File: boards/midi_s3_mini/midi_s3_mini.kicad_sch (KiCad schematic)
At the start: 35 parts, among them J1 Power2, J10 PLAY_CUE, J11 JOG, J12 TEMPO, J2 Power1, J3 UART_PI, J4 OneButtonA_TX, J5 OneButtonA_RX, J6 OneButtonB_RX, J7 OneButtonB_TX, J8 LOOP, J9 TRACK_ENC, U1 LOLIN_S3_Mini

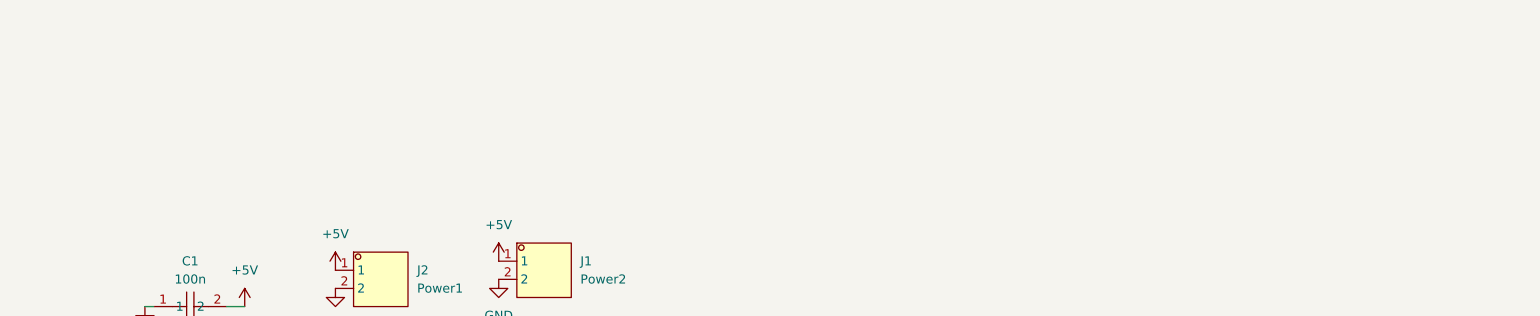
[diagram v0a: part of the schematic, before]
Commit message: Add notes and update schematic for main board ESD Schotky fix jog tch
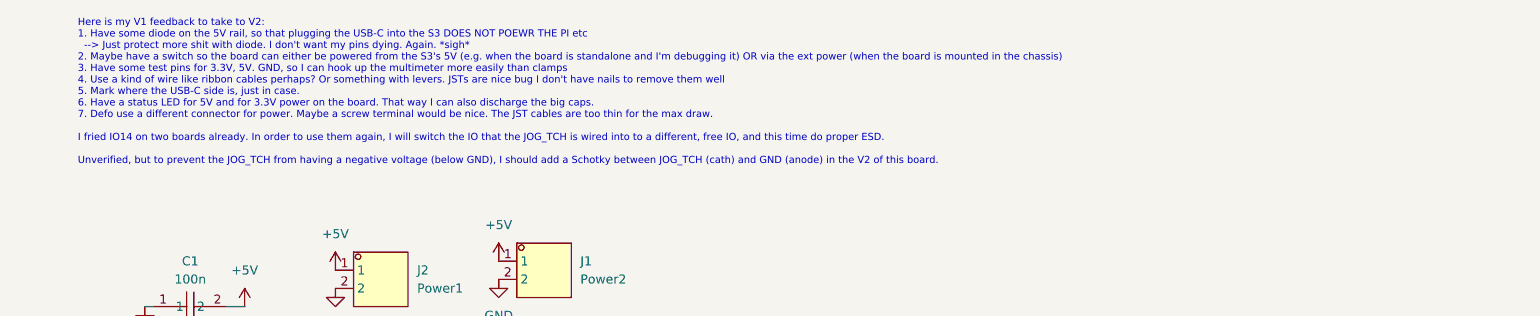
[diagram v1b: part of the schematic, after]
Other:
- note added: "Here is my V1 feedback to take to V2: 1. Have some diode on the 5V rail, so that plugging the USB-C into the S3 DOES NOT POEWR THE PI etc --> Just protect more shit with diode. I don't want my pins dying. Again. *sigh* 2. Maybe have a switch so the board can either be powered from the S3's 5V (e.g. when the board is standalone and I'm debugging it) OR via the ext power (when the board is mounted 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"
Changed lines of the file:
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@@
+		)
+	)
+	(text "Here is my V1 feedback to take to V2:\n1. Have some diode on the 5V rail, so that plugging the USB-C into the S3 DOES NOT POEWR THE PI etc\n  --> Just protect more shit with diode. I don't want my pins dying. Again. *sigh*\n2. Maybe have a switch so the board can either be powered from the S3's 5V (e.g. when the board is standalone and I'm debugging it) OR via the ext power (when the board is mounted in the chassis)\n3. Have some test pins for 3.3V, 5V. GND, so I can hook up the multimeter more easily than clamps\n4. Use a kind of wire like ribbon cables perhaps? Or something with levers. JSTs are nice bug I don't have nails to remove them well\n5. Mark where the USB-C side is, just in case.\n6. Have a status LED for 5V and for 3.3V power on the board. That way I can also discharge the big caps.\n7. Defo use a different connector for power. Maybe a screw terminal would be nice. The JST cables are too thin for the max draw.\n\nI fried IO14 on two boards already. In order to use them again, I will switch the IO that the JOG_TCH is wired into to a different, free IO, and this time do proper ESD.\n\nUnverified, but to prevent the JOG_TCH from having a negative voltage (below GND), I should add a Schotky between JOG_TCH (cath) and GND (anode) in the V2 of this board."
+		(exclude_from_sim no)
+		(at 24.892 -5.842 0)
+		(effects
+			(font
+				(size 1 1)
+			)
+			(justify left)
 		)
 	)

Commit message: Design the new power supply system
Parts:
- removed C1, C3: 100n, easyeda2kicad:CAP-TH_L4.2-W3.5-P2.54-D0.5, symbol easyeda2kicad:178MU0006
- removed C2: 1000uF / 35 V, easyeda2kicad:CAP-TH_BD10.0-P5.00-D1.0-FD, symbol easyeda2kicad:ERR1VM102G20OT
- removed C5: 10u / 50 V, easyeda2kicad:CAP-TH_BD5.0-P2.00-D0.8-FD, symbol easyeda2kicad:01EC1809SHC10UF50V
- removed C6: 22u 50V, easyeda2kicad:CAP-TH_BD5.0-P2.00-D0.5-FD, symbol easyeda2kicad:ERG50V22M5X11
- removed J1: Power2, easyeda2kicad:CONN-TH_S2B-PH-K-S-LF-SN, symbol easyeda2kicad:S2B-PH-K-S
- removed J2: Power1, easyeda2kicad:CONN-TH_S2B-PH-K-S-LF-SN, symbol easyeda2kicad:S2B-PH-K-S
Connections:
- net +3.3V: no longer U1.8 (3V3)
- net +5V: no longer U1.32 (VBUS)
- net JOG_TCH: no longer U1.16 (IO14)
- new net S3_3.3V: U1.8 (3V3)
- new net S3_VBUS_5V: U1.32 (VBUS)
- no-connect marks 5 -> 6
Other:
- added sheet Power (power.kicad_sch)
- note added: "I burnt IO14 on some boards, so for flexibility I will not use it"
- moved on the sheet: C4

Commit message: Add test points and leds
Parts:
- added TP3: VBUS_S3, symbol Connector:TestPoint
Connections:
- net S3_VBUS_5V: now also TP3.1
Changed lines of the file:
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@@
 		(color 0 0 0 0)
 	)
+	(junction
+		(at 134.62 78.74)
+		(diameter 0)
+		(color 0 0 0 0)
+	)
 	(no_connect
 		(at 100.33 78.74)
@@
 	(wire
 		(pts
+			(xy 134.62 78.74) (xy 133.35 78.74)
+		)
+		(stroke
+			(width 0)
+			(type default)
+		)
+	)
+	(wire
+		(pts
 			(xy 179.07 114.3) (xy 179.07 116.84)
 		)
@@
 	(wire
 		(pts
+			(xy 134.62 80.01) (xy 134.62 78.74)
+		)
+		(stroke
+			(width 0)
+			(type default)
+		)
+	)
+	(wire
+		(pts
 			(xy 69.85 129.54) (xy 72.39 129.54)
 		)
@@
 	(wire
 		(pts
+			(xy 135.89 78.74) (xy 134.62 78.74)
+		)
+		(stroke
+			(width 0)
+			(type default)
+		)
+	)
+	(wire
+		(pts
 			(xy 214.63 86.36) (xy 220.98 86.36)
 		)
@@
 	(global_label "S3_VBUS_5V"
 		(shape input)
-		(at 133.35 78.74 0)
+		(at 135.89 78.74 0)
 		(fields_autoplaced yes)
 		(effects
@@
 		)
 		(property "Intersheetrefs" "${INTERSHEET_REFS}"
-			(at 147.8861 78.74 0)
+			(at 150.4261 78.74 0)
 			(hide yes)
 			(show_name no)
@@
 					(unit 1)
 				)
+			)
+		)
+	)
+	(symbol
+		(lib_id "Connector:TestPoint")
+		(at 134.62 80.01 180)
+		(unit 1)
+		(body_style 1)
+		(exclude_from_sim no)
+		(in_bom yes)
+		(on_board yes)
+		(in_pos_files yes)
+		(dnp no)
+		(fields_autoplaced yes)
+		(property "Reference" "TP3"
+			(at 137.16 82.0419 0)
+			(show_name no)
+			(do_not_autoplace no)
+			(effects
+				(font
+					(size 1.27 1.27)
+				)
+				(justify right)
+			)
+		)
+		(property "Value" "VBUS_S3"
+			(at 137.16 84.5819 0)
+			(show_name no)
+			(do_not_autoplace no)
+			(effects
+				(font
+					(size 1.27 1.27)
+				)
+				(justify right)
+			)
+		)
+		(property "Footprint" ""
+			(at 129.54 80.01 0)
+			(hide yes)
+			(show_name no)
+			(do_not_autoplace no)
+			(effects
+				(font
+					(size 1.27 1.27)
+				)
+			)
+		)
+		(property "Datasheet" ""
+			(at 129.54 80.01 0)
+			(hide yes)
+			(show_name no)
+			(do_not_autoplace no)
+			(effects
+				(font
+					(size 1.27 1.27)
+				)
+			)
+		)
+		(property "Description" "test point"
+			(at 134.62 80.01 0)
+			(hide yes)
+			(show_name no)
+			(do_not_autoplace no)
+			(effects
+				(font
+					(size 1.27 1.27)
+				)
+			)
+		)
+		(pin "1"
+		)
+		(instances
+			(project "midi_s3_mini"
+				(path "/4a4c0c1b-df1c-48df-9685-1cfae0dce3a5"
+					(reference "TP3")
+					(unit 1)
+				)

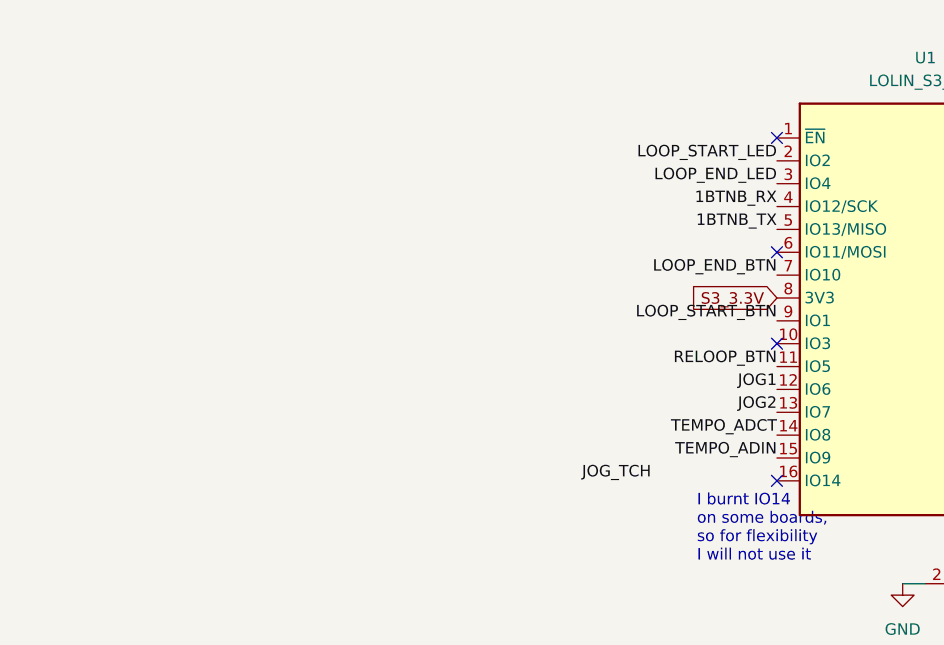
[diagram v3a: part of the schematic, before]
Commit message: Reassign JOG_TCH from IO14 --> IO11 on V2 boards
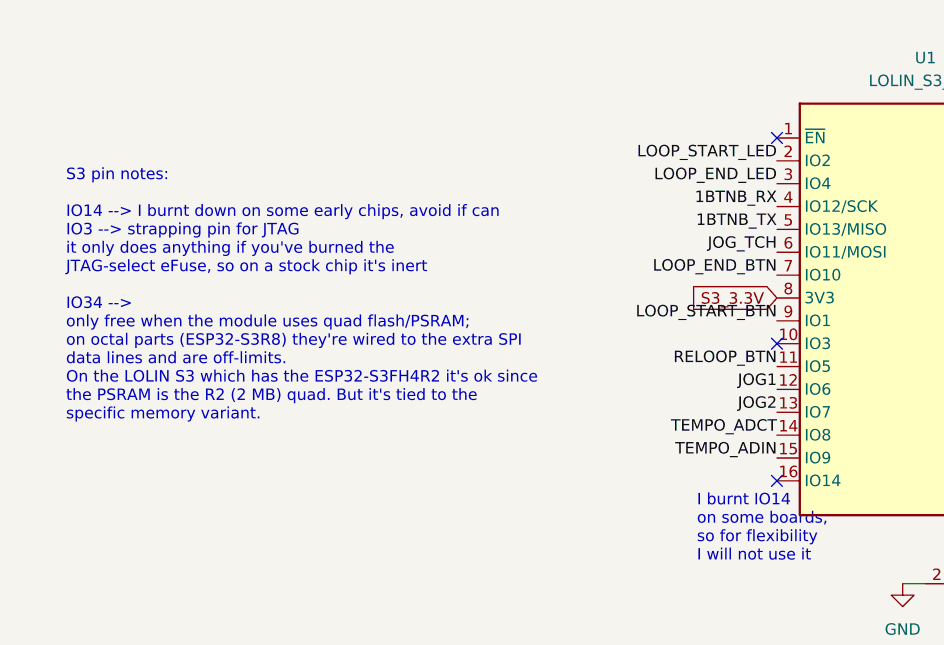
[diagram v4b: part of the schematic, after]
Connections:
- net JOG_TCH: now also U1.6 (IO11/MOSI)
- no-connect marks 6 -> 5
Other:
- note added: "S3 pin notes: IO14 --> I burnt down on some early chips, avoid if can IO3 --> strapping pin for JTAG it only does anything if you've burned the JTAG-select eFuse, so on a stock chip it's inert IO34 --> only free when the module uses quad flash/PSRAM; on octal parts (ESP32-S3R8) they're wired to the extra SPI data lines and are off-limits. On the LOLIN S3 which has the ESP32-S3FH4R2 it's ok since 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"
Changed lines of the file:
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@@
+		)
+	)
+	(text "S3 pin notes:\n\nIO14 --> I burnt down on some early chips, avoid if can\nIO3 --> strapping pin for JTAG\nit only does anything if you've burned the \nJTAG-select eFuse, so on a stock chip it's inert\n\nIO34 --> \nonly free when the module uses quad flash/PSRAM; \non octal parts (ESP32-S3R8) they're wired to the extra SPI \ndata lines and are off-limits.\nOn the LOLIN S3 which has the ESP32-S3FH4R2 it's ok since \nthe PSRAM is the R2 (2 MB) quad. But it's tied to the \nspecific memory variant. "
+		(exclude_from_sim no)
+		(at 21.336 58.166 0)
+		(effects
+			(font
+				(size 1.27 1.27)
+			)
+			(justify left)
 		)
 	)
@@
 	)
 	(no_connect
-		(at 100.33 53.34)
-	)
-	(no_connect
 		(at 133.35 73.66)
 	)
@@
 		)
 	)
+	(label "JOG_TCH"
+		(at 100.33 53.34 180)
+		(effects
+			(font
+				(size 1.27 1.27)
+			)
+			(justify right bottom)
+		)
+	)
 	(label "LED_CUE"
 		(at 133.35 133.35 180)
@@
 		(effects
 			(font
-				(size 1.27 1.27)
-			)
-			(justify right bottom)
-		)
-	)
-	(label "JOG_TCH"
-		(at 86.36 78.74 180)
-		(effects
-			(font

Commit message: Finish the ESD and power system for the V2 midi S3
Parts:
- removed C10, C11, C12, C13, C4, C7, C9: 100n, easyeda2kicad:CAP-TH_L4.2-W3.5-P2.54-D0.5, symbol easyeda2kicad:178MU0006
- removed J11: JOG, easyeda2kicad:CONN-TH_S5B-PH-K-S-LF-SN, symbol easyeda2kicad:S5B-PH-K-S-
- removed J3: UART_PI, easyeda2kicad:CONN-TH_3P-P2.00_S3B-PH-K-S-LF-SN, symbol easyeda2kicad:S3B-PH-K-S-
- added C10, C11, C2, C3, C5, C6, C8, C9: 100n s, easyeda2kicad:C0402, symbol easyeda2kicad:CL05B104KB54PNC
- added C4: 10nF ±10% 50V, easyeda2kicad:C0402, symbol easyeda2kicad:CL05B103KB5NNNC
- added J10: JOG, easyeda2kicad:CONN-TH_S5B-PH-K-S-LF-SN, symbol easyeda2kicad:S5B-PH-K-S-
- added J5: UART_PI, easyeda2kicad:CONN-TH_4P-P2.00_S4B-PH-K-S-LF-SN, symbol easyeda2kicad:S4B-PH-K-S-
- added R1, R10, R11, R12, R13, R14, R15, R16, R18, R19, R2, R20, R21, R22, R23, R24, R25, R26, R7, R8, R9: 1KΩ ±1%, easyeda2kicad:R0402, symbol easyeda2kicad:0402WGF1001TCE
- added TVS1, TVS2, TVS3, TVS4, TVS5, TVS6, TVS7, TVS8: SRV05-4, easyeda2kicad:SOT-23-6_L2.9-W1.6-P0.95-LS2.8-BL, symbol easyeda2kicad:SRV05-4_C558418
- renumbered C8 to C7, J4 to J1, J5 to J2, J6 to J3, J7 to J4, J9 to J6, J8 to J7, J10 to J8, J12 to J9, R5 to R17, R1 to R3, R2 to R4, R3 to R5, R4 to R6, TP3 to TP1
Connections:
- net +3.3V: now also C2.2, C6.2, C9.2, J10.3, TVS1.5, TVS2.5, TVS3.5, TVS4.5, TVS5.5, TVS6.5, TVS7.5, TVS8.5
- net +5V: now also C11.2
- net 1BTNA_RX: now also TVS1.1, TVS1.3
- net 1BTNA_TX: now also R1.1; no longer J1.2
- net 1BTNB_TX: now also R2.1; no longer J4.2
- net BTN_CUE: now also R21.1; no longer J8.4
- net BTN_PLAY: now also R18.1; no longer J8.2
- net ENC_CLK: now also C3.2, R12.1; no longer J6.5
- net ENC_DT: now also C5.2, R10.1; no longer J6.4
- net ENC_SW: now also C4.2, R9.1; no longer J6.3
- net GND: now also C10.1, C11.1, C2.1, C3.1, C4.1, C5.1, C6.1, C8.2, C9.1, J10.2, J5.1, J5.4, TVS1.2, TVS2.2, TVS3.2, TVS4.2, TVS5.2, TVS6.2, TVS7.2, TVS8.2
- net JOG1: now also R25.1
- net JOG2: now also R24.1
- net JOG_TCH: now also R20.1
- net LED_CUE: now also R22.1; no longer J8.5
- net LED_PLAY: now also R19.1; no longer J8.3
- net LOOP_END_BTN: now also R14.1; no longer J7.4
- net LOOP_END_LED: now also R15.1; no longer J7.5
- net LOOP_START_BTN: now also R11.1; no longer J7.2
- net LOOP_START_LED: now also R13.1; no longer J7.3
- net RELOOP_BTN: now also R16.1, TVS7.1; no longer J7.6
- net TEMPO_ADCT: now also C10.2, R26.1; no longer J9.2
- net TEMPO_ADIN: now also C8.1, R23.1; no longer J9.3
- net UART_RX_FROM_PI: now also R8.1
- net UART_TX_TO_PI: now also R7.1
- new net RAW_1BTNA_TX: J1.2, R1.2, TVS1.4
- new net RAW_1BTNB_TX: J4.2, R2.2, TVS1.6
- new net RAW_BTN_CUE: J8.4, R21.2, TVS8.3
- new net RAW_BTN_PLAY: J8.2, R18.2, TVS8.6
- new net RAW_ENC_CLK: J6.5, R12.2, TVS3.3
- new net RAW_ENC_DT: J6.4, R10.2, TVS3.6
- new net RAW_ENC_SW: J6.3, R9.2, TVS3.1
- new net RAW_JOG1: J10.5, R25.2, TVS6.1
- new net RAW_JOG2: J10.4, R24.2, TVS6.4
- new net RAW_JOG_TCH: J10.1, R20.2, TVS6.6
- new net RAW_LED_CUE: J8.5, R22.2, TVS8.1
- new net RAW_LED_PLAY: J8.3, R19.2, TVS8.4
- new net RAW_LOOP_END_BTN: J7.4, R14.2, TVS4.1
- new net RAW_LOOP_END_LED: J7.5, R15.2, TVS5.6
- new net RAW_LOOP_START_BTN: J7.2, R11.2, TVS4.6
- new net RAW_LOOP_START_LED: J7.3, R13.2, TVS5.4
- new net RAW_RELOOP_BTN: J7.6, R16.2, TVS4.4
- new net RAW_TEMPO_ADCT: J9.2, R26.2, TVS7.4
- new net RAW_TEMPO_ADIN: J9.3, R23.2, TVS7.6
- new net RAW_UART_RX_FROM_PI: J5.3, R8.2, TVS2.6
- new net RAW_UART_TX_TO_PI: J5.2, R7.2, TVS2.4
- no-connect marks 5 -> 13
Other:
- note added: "The LED_* here are controlling a MOSFET 2N7000's gate on the other side. They operate at 3.3V. The BTN_* on the other side are just a 100nF debounce cap and they close to GND, so we pull them up to 3.3V. The 5V is to power the LED, and the MOSFET open/closes the GND path on the power."
- note added: "This pinout matches the encoder's pinout if I mount a JST-PH angled on its bottom side. Enc is a KY-040"
- note removed: "This pinout matches the encoder's pinout if I mount a JST-PH angled on its bottom side"
- moved on the sheet: C7, J1, J2, J3, J4, J6, J7, J8, J9, R17, R3, R4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

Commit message: Footprint assignment for SMD assy
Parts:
- removed C7: 100n, easyeda2kicad:CAP-TH_L4.2-W3.5-P2.54-D0.5, symbol easyeda2kicad:178MU0006
- removed R17: 10k, easyeda2kicad:RES-TH_BD2.5-L6.5-P10.50-D0.6, symbol easyeda2kicad:MFR0W4F1002A50
- removed R3, R5: 1.8k, easyeda2kicad:RES-TH_BD2.4-L6.3-P10.30-D0.6, symbol easyeda2kicad:MFR-25FTE52-1K8
- removed R4, R6: 3.3k, easyeda2kicad:RES-TH_BD2.2-L6.5-P10.50-D0.6, symbol easyeda2kicad:MFR0W4F3301A50
- added C22: 100n, easyeda2kicad:C0402, symbol easyeda2kicad:CL05B104KB54PNC
- added R37, R40: 1.8KΩ ±1%, easyeda2kicad:R0603, symbol easyeda2kicad:0603WAF1801T5E
- added R38, R39: 3.3KΩ ±1%, easyeda2kicad:R0402, symbol easyeda2kicad:0402WGF3301TCE
- added R5: 10KΩ ±1%, easyeda2kicad:R0402, symbol easyeda2kicad:0402WGF1002TCE
- C1: renamed from C2; value 100n s -> 100n
- C10: renamed from C11; value 100n s -> 100n
- C2: renamed from C3; value 100n s -> 100n
- C4: renamed from C5; value 100n s -> 100n
- C5: renamed from C6; value 100n s -> 100n
- C7: renamed from C8; value 100n s -> 100n
- C8: renamed from C9; value 100n s -> 100n
- C9: renamed from C10; value 100n s -> 100n
- TP1: footprint (none) -> TestPoint:TestPoint_Pad_D2.5mm
- renumbered C4 to C3
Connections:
- net +3.3V: now also R5.2
- net 1BTNA_RX: now also R37.1, R38.2
- net 1BTNB_RX: now also R39.2, R40.1
- net GND: now also C22.1, R38.1, R39.1
- net JOG_TCH: now also C22.2, R5.1
- net at J2.2: now also R37.2
- net at J3.2: now also R40.2

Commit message: Last tiny net fixes before PCB traces
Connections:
- net 1BTNA_RX: no longer TVS1.3
- net 1BTNB_RX: now also TVS1.3
- net RELOOP_BTN: no longer TVS7.1
- no-connect marks 13 -> 14
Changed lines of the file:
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@@
+	)
+	(no_connect
+		(at 76.2 278.13)
 	)
 	(no_connect
@@
 		)
 	)
-	(label "RELOOP_BTN"
-		(at 76.2 278.13 180)
-		(effects
-			(font
-				(size 1.27 1.27)
-			)
-			(justify right bottom)
-		)
-	)
 	(label "JOG_TCH"
 		(at 100.33 53.34 180)
@@
 		)
 	)
+	(label "1BTNB_RX"
+		(at 246.38 80.01 0)
+		(effects
+			(font
+				(size 1.27 1.27)
+			)
+			(justify left bottom)
+		)
+	)
 	(label "RAW_LOOP_END_BTN"
 		(at 118.11 180.34 180)
@@
 		)
 	)
-	(label "1BTNA_RX"
-		(at 246.38 80.01 0)
-		(effects
-			(font
-				(size 1.27 1.27)
-			)
-			(justify left bottom)
-		)
-	)

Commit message: Lay down PCB with no GND plane breaks
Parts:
- added FID1, FID2, FID3: Fiducial, Fiducial:Fiducial_1mm_Mask2mm, symbol Mechanical:Fiducial
- added TVS2: SRV05-4, easyeda2kicad:SOT-23-6_L2.9-W1.6-P0.95-LS2.8-BL, symbol easyeda2kicad:SRV05-4_C558418
- renumbered C22 to C6, R5 to R17, R37 to R3, R38 to R4, R40 to R5, R39 to R6, TVS2 to TVS3, TVS3 to TVS4, TVS4 to TVS5, TVS5 to TVS6, TVS6 to TVS7, TVS7 to TVS8, TVS8 to TVS9
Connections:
- net +3.3V: now also TVS2.5
- net 1BTNB_RX: now also TVS2.3; no longer TVS1.3
- net GND: now also TVS2.2
- net RAW_1BTNA_TX: now also TVS1.6; no longer TVS1.4
- net RAW_1BTNB_TX: now also TVS2.4; no longer TVS1.6
- net RAW_BTN_CUE: now also TVS9.4; no longer TVS9.3
- net RAW_BTN_PLAY: now also TVS9.1; no longer TVS9.6
- net RAW_ENC_DT: now also TVS4.1; no longer TVS4.6
- net RAW_ENC_SW: now also TVS4.6; no longer TVS4.1
- net RAW_JOG1: now also TVS7.3; no longer TVS7.1
- net RAW_LED_CUE: now also TVS9.6; no longer TVS9.1
- net RAW_LED_PLAY: now also TVS9.3; no longer TVS9.4
- net RAW_LOOP_END_BTN: now also TVS6.6; no longer TVS5.1
- net RAW_LOOP_END_LED: now also TVS5.6; no longer TVS6.6
- net RAW_LOOP_START_BTN: now also TVS6.3; no longer TVS5.6
- net RAW_RELOOP_BTN: now also TVS5.1; no longer TVS5.4
- net RAW_TEMPO_ADCT: now also TVS8.6; no longer TVS8.4
- net RAW_TEMPO_ADIN: now also TVS8.1; no longer TVS8.6
- net RAW_UART_RX_FROM_PI: now also TVS3.1; no longer TVS3.6
- net RAW_UART_TX_TO_PI: now also TVS3.6; no longer TVS3.4
- no-connect marks 14 -> 18
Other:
- moved on the sheet: R1, R2
